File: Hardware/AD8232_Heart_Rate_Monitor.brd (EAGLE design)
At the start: 35.6 x 27.9 mm, 38 parts, among them U1 AD8232

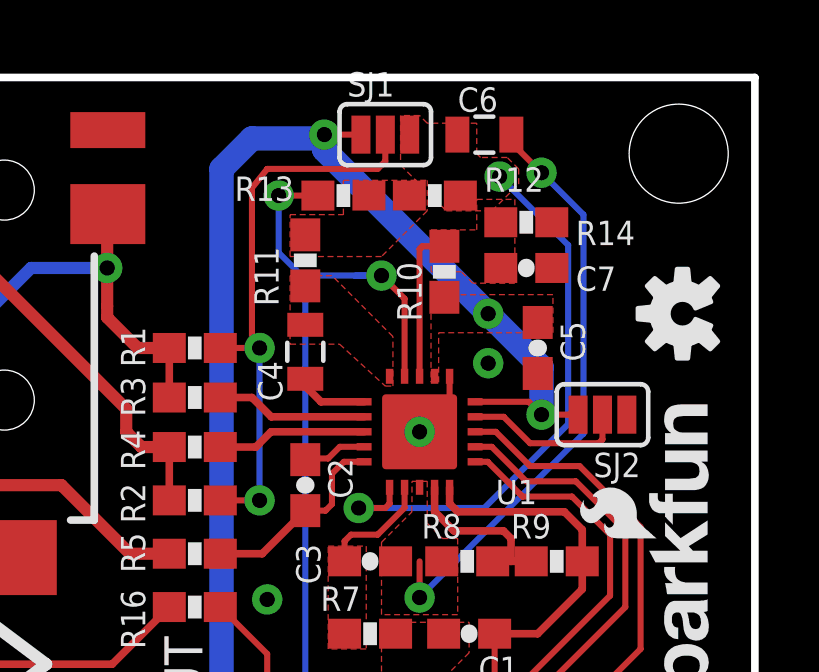
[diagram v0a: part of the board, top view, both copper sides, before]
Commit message: changed jumpers to populatable jumpers makes for easy production changes
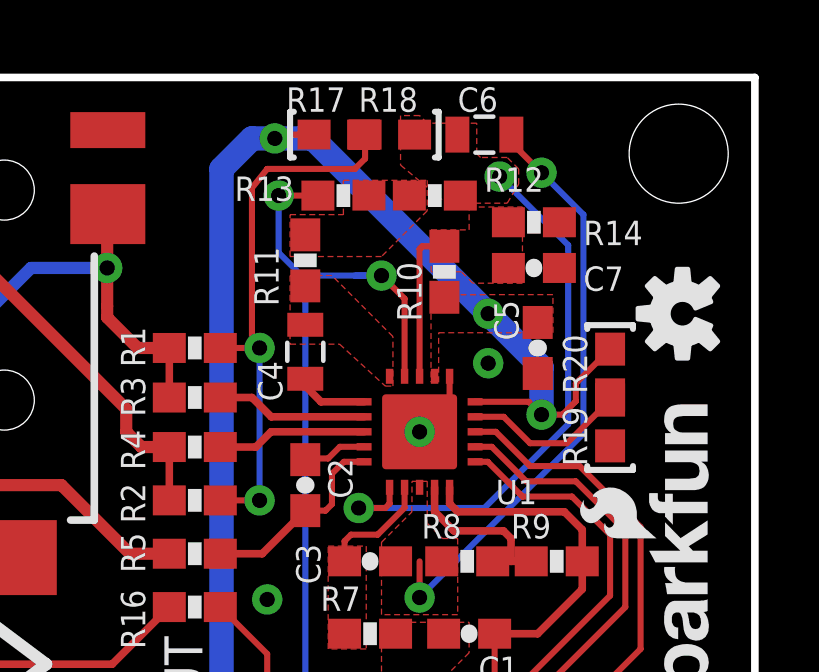
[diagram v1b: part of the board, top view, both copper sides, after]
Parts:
- removed SJ1, SJ2: (no value), SparkFun-Passives:SJ_3_PASTE1&2
- added R17, R19: 0, SparkFun-Resistors:0603
- added R18, R20: DNP, SparkFun-Resistors:0603
- moved C7 0.25 mm to (28.2, 21.6)
- moved R14 0.25 mm to (28.2, 23.1)
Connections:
- removed net N$21: SJ2.2, U1.14
- new net N$11: R19.2, R20.1, U1.14
- net 3.3V: now also R17.1, R20.2; no longer SJ1.1, SJ2.3
- net GND: now also R19.1; no longer SJ2.1
- net N$16: now also R18.2; no longer SJ1.3
- net N$20: now also R17.2, R18.1; no longer SJ1.2
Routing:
- net N$11: track 0.00 -> 5.64 mm
- net N$21: track 5.49 -> 0.00 mm
- net 3.3V: track 59.1 -> 61.1 mm
- net N$20: track 18.9 -> 18.2 mm

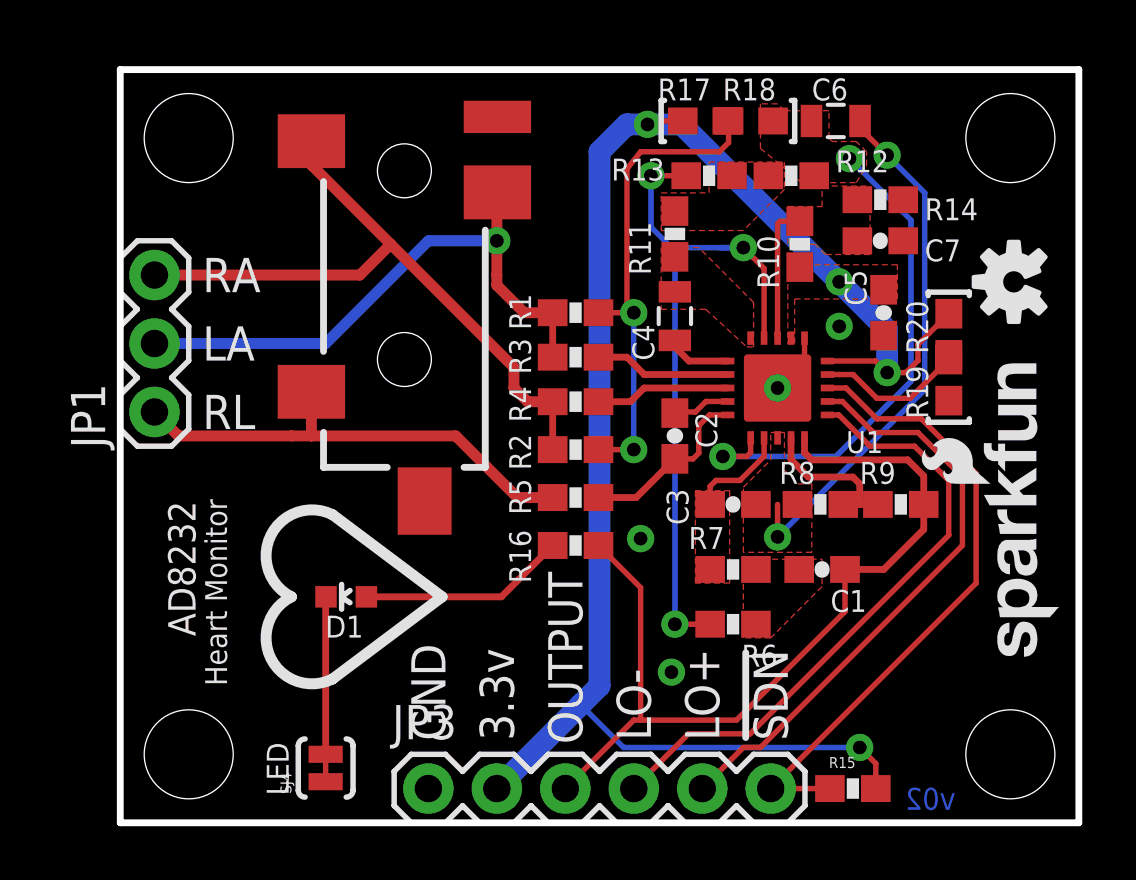
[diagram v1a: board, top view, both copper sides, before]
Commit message: added matched traces
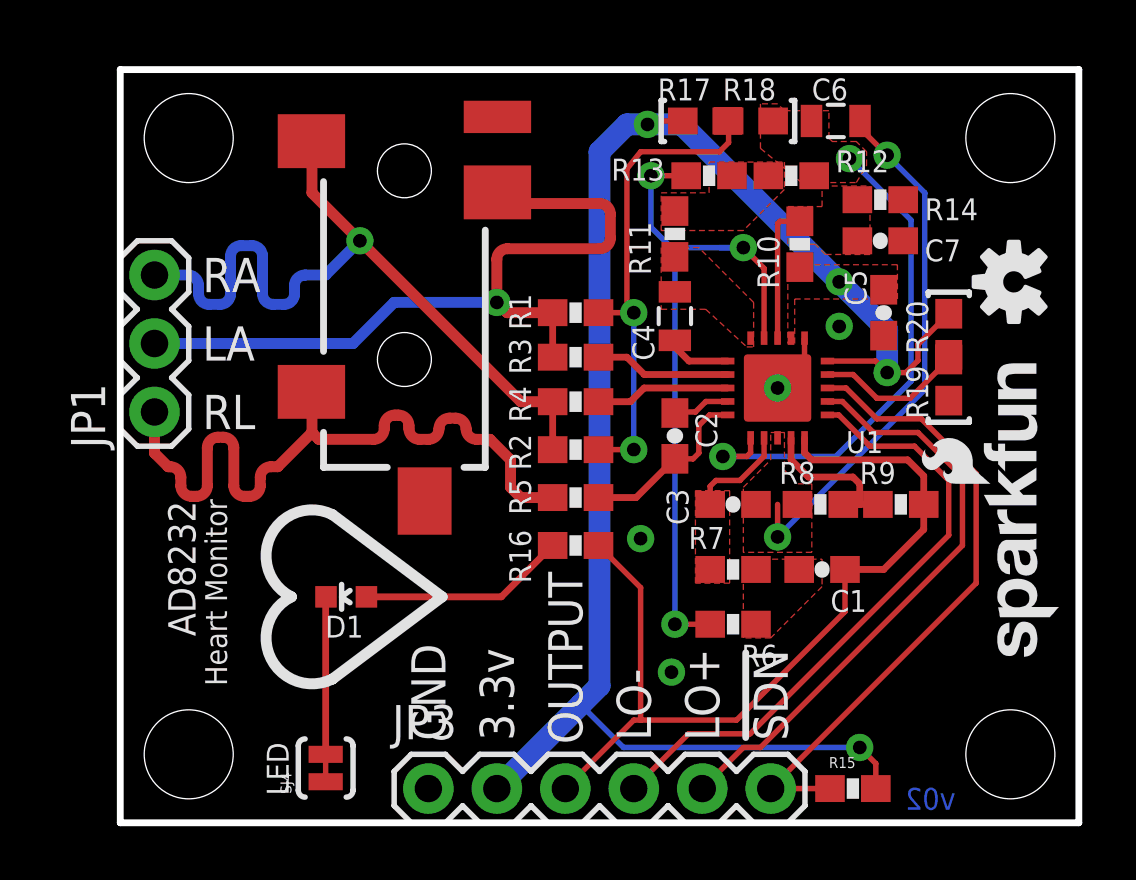
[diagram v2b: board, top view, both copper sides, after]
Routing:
- net RL: track 17.7 -> 26.4 mm
- net LA: track 21.9 -> 28.8 mm
- net RA: track 24.9 -> 28.7 mm, vias 0 -> 1

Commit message: Changed layout in attempt to remove noise.  Changed resistor values to help remove DC offset.
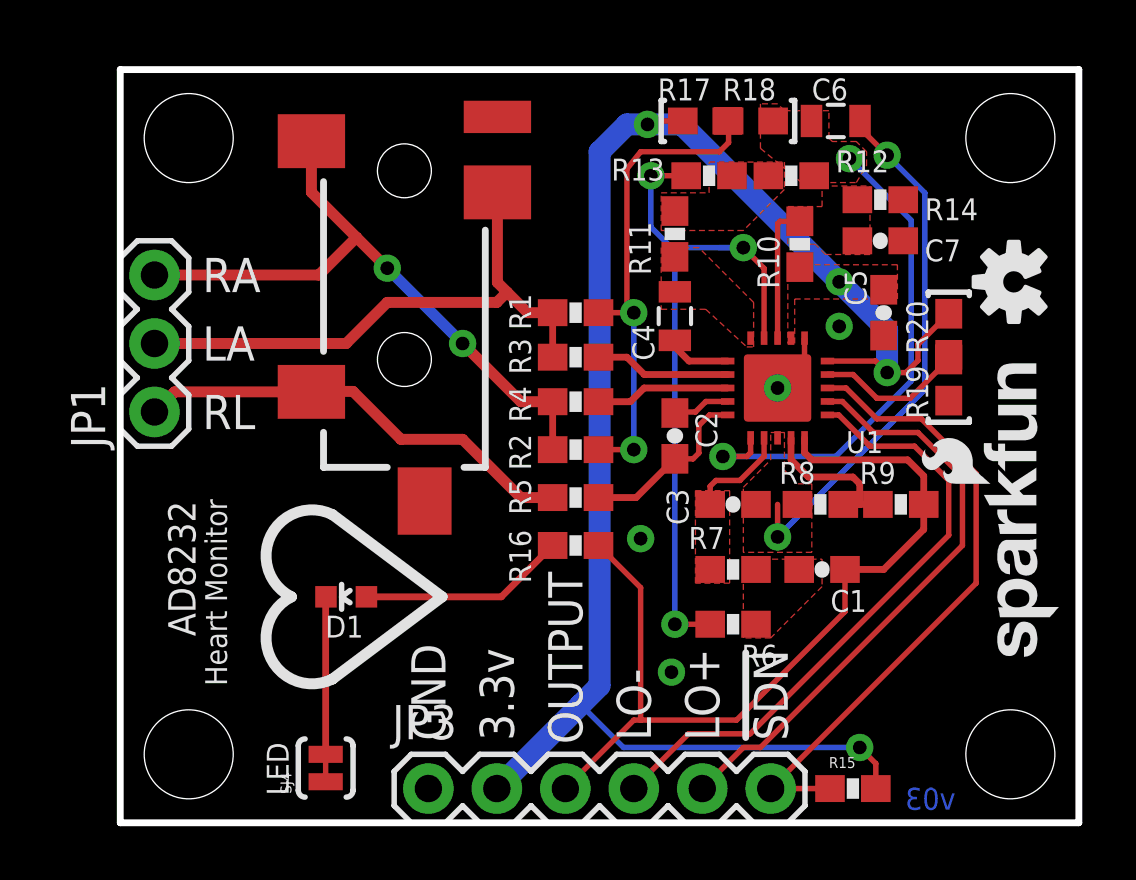
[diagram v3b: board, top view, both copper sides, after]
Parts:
- R13: value 1.4M -> 10M
- R15: value (none) -> 10K
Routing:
- net RL: track 26.4 -> 16.7 mm
- net LA: track 28.8 -> 21.4 mm, vias 1 -> 0
- net RA: track 28.7 -> 23.9 mm, vias 1 -> 2
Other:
- board text added: "v03"
- board text removed: "v02"

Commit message: Added fiducials
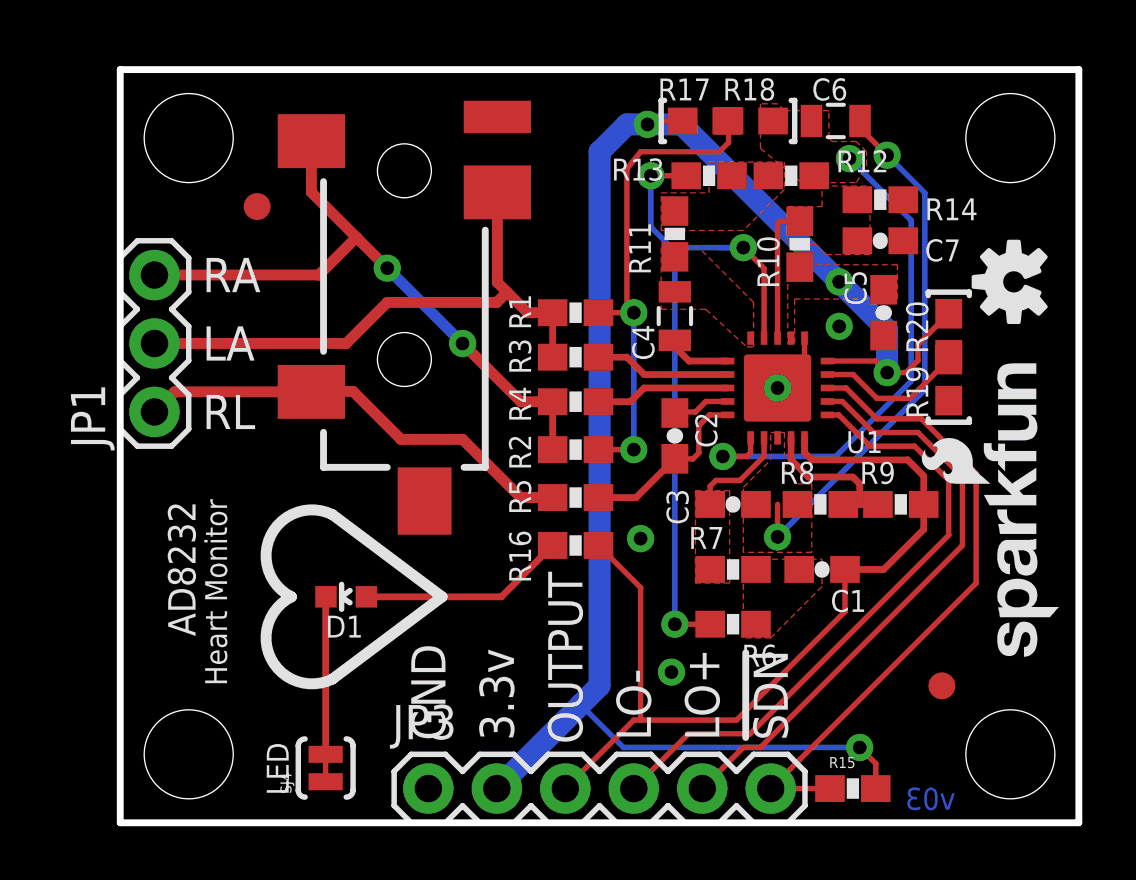
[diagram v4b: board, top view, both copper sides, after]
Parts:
- added FID1, FID2: FIDUCIAL1X2, SparkFun-Aesthetics:FIDUCIAL-1X2
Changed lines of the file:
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@@
 <setting verticaltext="up"/>
 </settings>
-<grid distance="0.01" unitdist="inch" unit="inch" style="lines" multiple="1" display="yes" altdistance="0.005" altunitdist="inch" altunit="inch"/>
+<grid distance="0.05" unitdist="inch" unit="inch" style="lines" multiple="1" display="yes" altdistance="0.01" altunitdist="inch" altunit="inch"/>
 <layers>
 <layer number="1" name="Top" color="4" fill="1" visible="yes" active="yes"/>
@@
 <layer number="18" name="Vias" color="2" fill="1" visible="yes" active="yes"/>
 <layer number="19" name="Unrouted" color="6" fill="1" visible="yes" active="yes"/>
-<layer number="20" name="Dimension" color="15" fill="1" visible="yes" active="yes"/>
-<layer number="21" name="tPlace" color="16" fill="1" visible="yes" active="yes"/>
-<layer number="22" name="bPlace" color="14" fill="1" visible="yes" active="yes"/>
+<layer number="20" name="Dimension" color="6" fill="1" visible="yes" active="yes"/>
+<layer number="21" name="tPlace" color="6" fill="1" visible="yes" active="yes"/>
+<layer number="22" name="bPlace" color="6" fill="1" visible="yes" active="yes"/>
 <layer number="23" name="tOrigins" color="15" fill="1" visible="yes" active="yes"/>
 <layer number="24" name="bOrigins" color="15" fill="1" visible="yes" active="yes"/>
@@
 <attribute name="VALUE" x="31.877" y="17.018" size="0.4064" layer="27" font="vector" rot="R90"/>
 </element>
+<element name="FID1" library="SparkFun-Aesthetics" package="FIDUCIAL-1X2" value="FIDUCIAL1X2" x="5.08" y="22.86"/>
+<element name="FID2" library="SparkFun-Aesthetics" package="FIDUCIAL-1X2" value="FIDUCIAL1X2" x="30.48" y="5.08"/>
 </elements>
 <signals>

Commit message: fixed Rev Numbers
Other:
- board text added: "v10"
- board text removed: "v03"
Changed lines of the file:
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@@
 <text x="16.51" y="2.921" size="1.27" layer="21" font="vector" ratio="20" rot="R90" align="center-left">OUTPUT</text>
 <text x="16.51" y="2.921" size="1.27" layer="22" font="vector" ratio="20" rot="MR90" align="center-left">OUTPUT</text>
-<text x="30.988" y="0.889" size="0.8128" layer="16" font="vector" ratio="20" rot="MR0" align="center-left">v03</text>
+<text x="30.988" y="0.889" size="0.8128" layer="16" font="vector" ratio="20" rot="MR0" align="center-left">v10</text>
 <text x="3.048" y="17.78" size="1.27" layer="21" font="vector" ratio="15" align="center-left">LA</text>
 <text x="3.048" y="20.32" size="1.27" layer="21" font="vector" ratio="15" align="center-left">RA</text>
